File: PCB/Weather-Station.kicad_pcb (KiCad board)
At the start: 2 copper layers, 60 x 31.5 mm, 38 parts, among them J1 Biruta, J2 Power, J3 BH1750-FVI, J4 BME280, J5 Pluviometro, J6 Anemometro, J7 FTDI, J8 Conn_01x02, J9 Conn_01x02, SW1 SW_Push_SPDT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

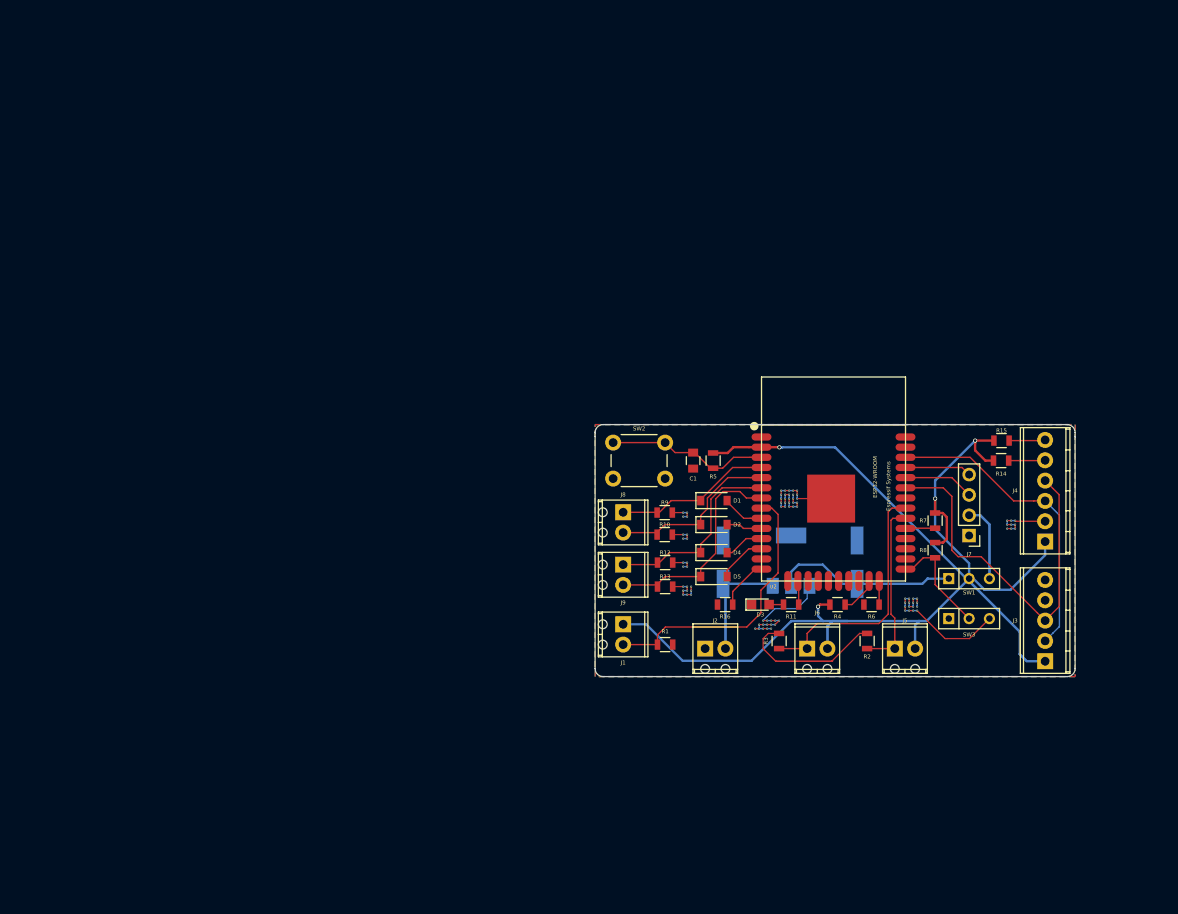
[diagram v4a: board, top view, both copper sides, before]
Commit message: Alterando as PCBs da estação para usar os ADCs e o DataLogger
Signed-off-by: Gustavo Costa <gustavocosta@ic.ufal.br>
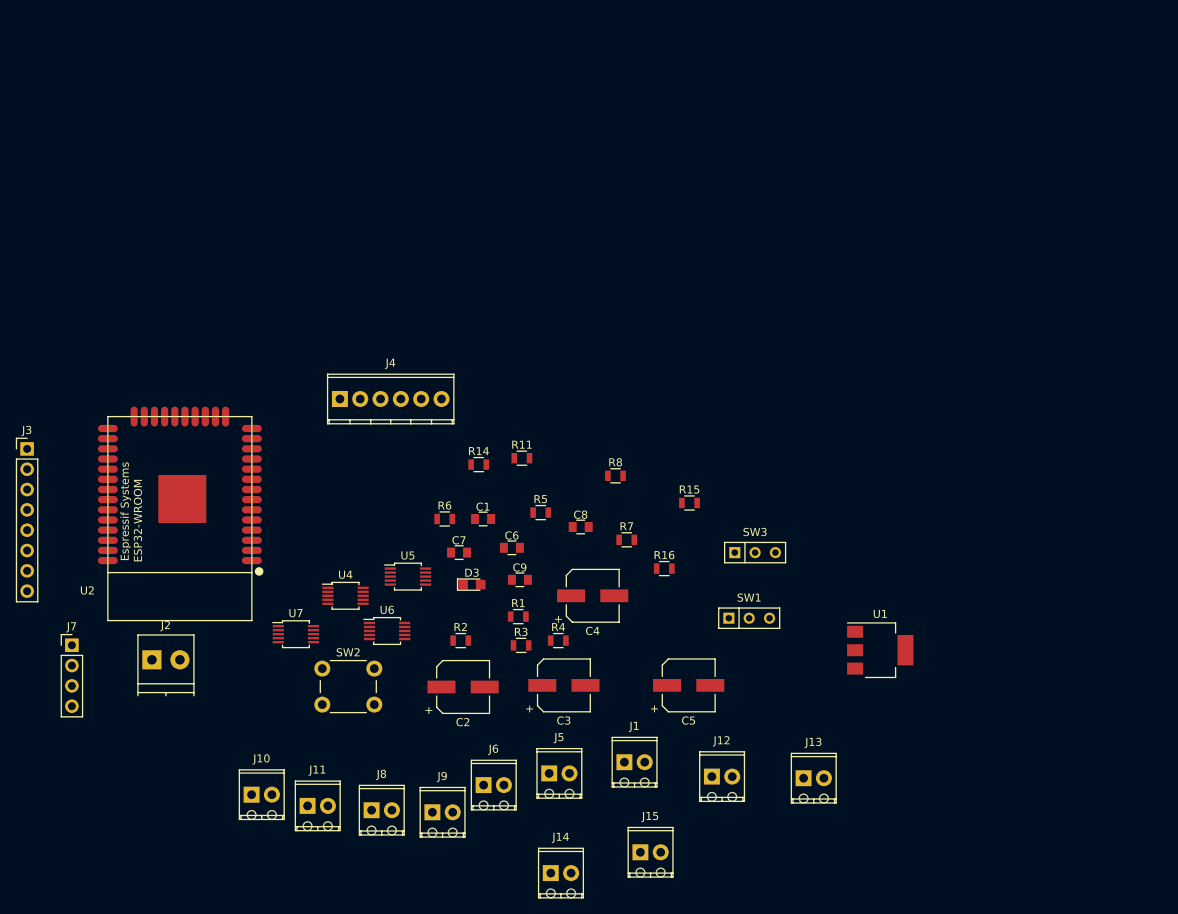
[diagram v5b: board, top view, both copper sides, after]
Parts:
- removed D1, D2, D4, D5: D, Diodes_SMD:D_SOD-123
- removed R10, R12, R13, R9: 1.5K, Resistors_SMD:R_0805
- added C4: 22μF, Capacitors_SMD:CP_Elec_6.3x7.7, F.Cu at (164.7, 102.4)
- added C5: 22μF, Capacitors_SMD:CP_Elec_6.3x7.7, F.Cu at (176.7, 113.6)
- added C6: 0.1uF, Capacitors_SMD:C_0805, F.Cu at (154.6, 96.4)
- added C7: 0.1uF, Capacitors_SMD:C_0805, F.Cu at (148.0, 97.0)
- added C8: 0.1uF, Capacitors_SMD:C_0805, F.Cu at (163.2, 93.8)
- added C9: 0.1uF, Capacitors_SMD:C_0805, F.Cu at (155.6, 100.4)
- added J10: Conn_01x02, TerminalBlock_Phoenix:TerminalBlock_Phoenix_MPT-2.54mm_2pol, F.Cu at (122.1, 127.3)
- added J11: Conn_01x02, TerminalBlock_Phoenix:TerminalBlock_Phoenix_MPT-2.54mm_2pol, F.Cu at (129.1, 128.7)
- added J12: Conn_01x02, TerminalBlock_Phoenix:TerminalBlock_Phoenix_MPT-2.54mm_2pol, F.Cu at (179.6, 125.0)
- added J13: Conn_01x02, TerminalBlock_Phoenix:TerminalBlock_Phoenix_MPT-2.54mm_2pol, F.Cu at (191.1, 125.2)
- added J14: Conn_01x02, TerminalBlock_Phoenix:TerminalBlock_Phoenix_MPT-2.54mm_2pol, F.Cu at (159.5, 137.1)
- added J15: Conn_01x02, TerminalBlock_Phoenix:TerminalBlock_Phoenix_MPT-2.54mm_2pol, F.Cu at (170.7, 134.5)
- added U4: ADS1115, Housings_SSOP:MSOP-10_3x3mm_Pitch0.5mm, F.Cu at (133.8, 102.4)
- added U5: ADS1115, Housings_SSOP:MSOP-10_3x3mm_Pitch0.5mm, F.Cu at (141.6, 100.0)
- added U6: ADS1115, Housings_SSOP:MSOP-10_3x3mm_Pitch0.5mm, F.Cu at (139.0, 106.8)
- added U7: ADS1115, Housings_SSOP:MSOP-10_3x3mm_Pitch0.5mm, F.Cu at (127.6, 107.2)
- C2, C3, U1: moved to F.Cu
- J2: footprint TerminalBlock_Phoenix:TerminalBlock_Phoenix_MPT-2.54mm_2pol -> TerminalBlock_Phoenix:TerminalBlock_Phoenix_PT-3.5mm_2pol
- J3: value BH1750-FVI -> DataLogger; footprint TerminalBlock_Phoenix:TerminalBlock_Phoenix_MPT-2.54mm_5pol -> Pin_Headers:Pin_Header_Straight_1x08_Pitch2.54mm
- moved J3 130.0 mm to (94.0, 84.0), turned to 0 degrees
- moved J7 113.0 mm to (99.6, 108.6), turned to 0 degrees
- moved J4 89.9 mm to (133.1, 77.8), turned to 0 degrees
- moved U2 81.9 mm to (113.1, 92.8), turned to 0 degrees
- moved J2 69.2 mm to (109.6, 110.4)
- moved R14 65.3 mm to (150.4, 86.0), turned to 0 degrees
- moved R6 54.4 mm to (146.2, 92.8), turned to 0 degrees
- moved R2 50.8 mm to (148.2, 108.0), turned to 0 degrees
- moved J8 48.7 mm to (137.1, 129.2), turned to 0 degrees
- moved SW2 46.0 mm to (130.9, 111.5)
- moved J5 45.9 mm to (159.3, 124.6)
- moved J6 43.9 mm to (151.1, 126.1)
- moved R8 41.0 mm to (167.6, 87.4), turned to 0 degrees
- moved R15 39.8 mm to (176.8, 90.8), turned to 0 degrees
- moved C3 39.8 mm to (161.1, 113.6), turned to 0 degrees
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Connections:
- net ADC1_CH4 renamed Net-(J1-Pad2)
- J3 pad 1: +3V3 -> CS
- J3 pad 2: Net-(J3-Pad2) -> MOSI
- J3 pad 3: Net-(J3-Pad3) -> MISO
- J3 pad 4: (no net) -> SCK
- J3 pad 5: GND -> SCL
- J4 pad 3: Net-(J3-Pad2) -> SCL
- J4 pad 4: Net-(J3-Pad3) -> SDA
- J8 pad 1: ADC1_CH0 -> Net-(J8-Pad1)
- J8 pad 2: ADC1_CH3 -> Net-(J8-Pad2)
- J9 pad 1: ADC1_CH6 -> Net-(J9-Pad1)
- J9 pad 2: ADC1_CH7 -> Net-(J9-Pad2)
- SW3 pad 1: (no net) -> Net-(SW3-Pad1)
- U2 pad 10: GPIO25 -> Net-(J6-Pad1)
- U2 pad 11: GPIO26 -> Net-(U2-Pad11)
- U2 pad 12: GPIO27 -> Net-(U2-Pad12)
- U2 pad 13: (no net) -> Net-(U2-Pad13)
- U2 pad 17: (no net) -> Net-(U2-Pad17)
- U2 pad 18: (no net) -> Net-(U2-Pad18)
- U2 pad 19: (no net) -> Net-(U2-Pad19)
- U2 pad 20: (no net) -> Net-(U2-Pad20)
- U2 pad 21: (no net) -> Net-(U2-Pad21)
- U2 pad 22: (no net) -> Net-(U2-Pad22)
- U2 pad 26: (no net) -> Net-(U2-Pad26)
- U2 pad 27: (no net) -> Net-(U2-Pad27)
- U2 pad 28: (no net) -> CS
- U2 pad 30: Net-(J5-Pad1) -> SCK
- U2 pad 31: Net-(J6-Pad1) -> MISO
- U2 pad 32: (no net) -> Net-(U2-Pad32)
- U2 pad 33: Net-(J3-Pad3) -> SDA
- U2 pad 36: Net-(J3-Pad2) -> SCL
- U2 pad 37: (no net) -> MOSI
- U2 pad 4: ADC1_CH0 -> Net-(U2-Pad4)
- U2 pad 5: ADC1_CH3 -> Net-(U2-Pad5)
- U2 pad 6: ADC1_CH6 -> Net-(U2-Pad6)
- U2 pad 7: ADC1_CH7 -> Net-(U2-Pad7)
- U2 pad 9: GPIO33 -> Net-(J5-Pad1)
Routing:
- net +3V3: track 165.8 -> 0.00 mm, vias 4 -> 0
- net GND: track 91.7 -> 0.00 mm, vias 86 -> 0
- net Net-(J3-Pad3): track 47.2 -> 0.00 mm
- net Net-(J3-Pad2): track 38.7 -> 0.00 mm
- net Net-(J1-Pad2): track 35.2 -> 0.00 mm
- net Net-(J6-Pad1): track 31.7 -> 0.00 mm
- net ADC1_CH7: track 27.4 -> 0.00 mm
- net ADC1_CH6: track 24.5 -> 0.00 mm
- net Net-(C3-Pad1): track 23.1 -> 0.00 mm
- net ADC1_CH3: track 22.0 -> 0.00 mm
- net Net-(J5-Pad1): track 21.6 -> 0.00 mm
- net Net-(C1-Pad2): track 20.5 -> 0.00 mm
- net ADC1_CH0: track 19.7 -> 0.00 mm
- net Net-(C2-Pad1): track 14.5 -> 0.00 mm
- net Net-(R8-Pad1): track 13.6 -> 0.00 mm
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- removed copper zone on B.Cu, net GND
- removed copper zone on F.Cu, net GND
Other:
- board outline removed

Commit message: Iniciado PCB
Signed-off-by: Gustavo Costa <gustavocosta@ic.ufal.br>
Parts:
- added U3: AP1117-33, TO_SOT_Packages_SMD:SOT-223, B.Cu at (143.8, 62.8)
- C2, C3, C4, C5, J3, U1: moved to B.Cu
- moved J7 89.8 mm to (180.8, 70.2), turned to 270 degrees
- moved J3 86.2 mm to (179.9, 76.5), turned to 90 degrees
- moved J1 74.9 mm to (126.2, 61.5), turned to 270 degrees
- moved J5 64.1 mm to (126.2, 69.7), turned to 270 degrees
- moved U1 61.0 mm to (143.8, 87.2)
- moved SW2 55.0 mm to (131.2, 56.5), turned to 180 degrees
- moved J6 54.4 mm to (126.2, 77.7), turned to 270 degrees
- moved C5 54.1 mm to (143.8, 70.8)
- moved U7 53.3 mm to (179.7, 95.8)
- moved U2 52.9 mm to (151.8, 56.8), turned to 180 degrees
- moved J4 52.6 mm to (184.0, 64.7), turned to 90 degrees
- moved C4 52.3 mm to (143.8, 54.5)
- moved SW1 49.4 mm to (171.2, 57.5), turned to 180 degrees
- moved R1 49.0 mm to (137.9, 59.2), turned to 180 degrees
- moved R3 48.0 mm to (138.0, 64.0), turned to 180 degrees
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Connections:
- SW3 pad 1: Net-(SW3-Pad1) -> (no net)
- U2 pad 11: Net-(U2-Pad11) -> (no net)
- U2 pad 12: Net-(U2-Pad12) -> (no net)
- U2 pad 13: Net-(U2-Pad13) -> (no net)
- U2 pad 17: Net-(U2-Pad17) -> (no net)
- U2 pad 18: Net-(U2-Pad18) -> (no net)
- U2 pad 19: Net-(U2-Pad19) -> (no net)
- U2 pad 20: Net-(U2-Pad20) -> (no net)
- U2 pad 21: Net-(U2-Pad21) -> (no net)
- U2 pad 22: Net-(U2-Pad22) -> (no net)
- U2 pad 26: Net-(U2-Pad26) -> (no net)
- U2 pad 27: Net-(U2-Pad27) -> (no net)
- U2 pad 32: Net-(U2-Pad32) -> (no net)
- U2 pad 4: Net-(U2-Pad4) -> (no net)
- U2 pad 5: Net-(U2-Pad5) -> (no net)
- U2 pad 6: Net-(U2-Pad6) -> (no net)
- U2 pad 7: Net-(U2-Pad7) -> (no net)
- U4 pad 2: Net-(U4-Pad2) -> (no net)
- U5 pad 2: Net-(U5-Pad2) -> (no net)
- U6 pad 2: Net-(U6-Pad2) -> (no net)
- U7 pad 2: Net-(U7-Pad2) -> (no net)
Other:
- board outline added: 65 x 60 mm

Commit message: Fazendo pcb
Signed-off-by: Gustavo Costa <gustavocosta@ic.ufal.br>
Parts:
- added R10: 10k, Resistors_SMD:R_0805, F.Cu at (160.8, 82.2)
- added R9: 10k, Resistors_SMD:R_0805, F.Cu at (160.8, 86.5)
- moved C2 24.8 mm to (143.8, 54.5)
- moved C3 24.8 mm to (143.8, 70.8)
- moved U1 24.8 mm to (143.8, 62.5)
- moved C4 24.5 mm to (143.8, 79.0)
- moved C5 24.5 mm to (143.8, 95.2)
- moved U3 24.5 mm to (143.8, 87.2)
- moved SW3 20.1 mm to (169.2, 72.5), turned to 0 degrees
- moved J7 19.0 mm to (174.0, 52.5)
- moved SW1 16.4 mm to (178.0, 72.5), turned to 0 degrees
- moved R7 1.00 mm to (165.5, 63.0)
- moved R8 1.00 mm to (165.5, 68.0)
- moved R3 0.25 mm to (138.0, 64.2)
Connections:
- U4 pad 4: Net-(J8-Pad2) -> Net-(J8-Pad1)
- U4 pad 5: Net-(J8-Pad1) -> Net-(J8-Pad2)
- U4 pad 6: Net-(J9-Pad2) -> Net-(J9-Pad1)
- U4 pad 7: Net-(J9-Pad1) -> Net-(J9-Pad2)
- U5 pad 4: Net-(J10-Pad2) -> Net-(J10-Pad1)
- U5 pad 5: Net-(J10-Pad1) -> Net-(J10-Pad2)
- U5 pad 6: Net-(J11-Pad2) -> Net-(J11-Pad1)
- U5 pad 7: Net-(J11-Pad1) -> Net-(J11-Pad2)
- U6 pad 4: Net-(J12-Pad2) -> Net-(J12-Pad1)
- U6 pad 5: Net-(J12-Pad1) -> Net-(J12-Pad2)
- U6 pad 6: Net-(J13-Pad2) -> Net-(J13-Pad1)
- U6 pad 7: Net-(J13-Pad1) -> Net-(J13-Pad2)
- U7 pad 4: Net-(J14-Pad2) -> Net-(J14-Pad1)
- U7 pad 5: Net-(J14-Pad1) -> Net-(J14-Pad2)
- U7 pad 6: Net-(J15-Pad2) -> Net-(J15-Pad1)
- U7 pad 7: Net-(J15-Pad1) -> Net-(J15-Pad2)
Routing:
- net Net-(C2-Pad1): track 0.00 -> 63.1 mm
- net Net-(J6-Pad1): track 0.00 -> 24.0 mm
- net +5V: track 0.00 -> 23.2 mm
- net Net-(J5-Pad1): track 0.00 -> 19.9 mm
- net Net-(C1-Pad2): track 0.00 -> 19.6 mm
- net Net-(J1-Pad2): track 0.00 -> 19.0 mm
- net Net-(J14-Pad1): track 0.00 -> 13.1 mm
- net Net-(J13-Pad2): track 0.00 -> 12.4 mm
- net Net-(J8-Pad1): track 0.00 -> 12.3 mm
- net Net-(J15-Pad2): track 0.00 -> 12.0 mm
- net Net-(J9-Pad2): track 0.00 -> 11.9 mm
- net Net-(J12-Pad1): track 0.00 -> 11.9 mm
- net Net-(J10-Pad1): track 0.00 -> 11.8 mm
- net Net-(J11-Pad2): track 0.00 -> 11.8 mm
- net Net-(C3-Pad1): track 0.00 -> 10.9 mm
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
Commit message: Finalizando PCB
Signed-off-by: Gustavo <gustavocosta@ic.ufal.br>
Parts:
- moved SW1 13.6 mm to (173.2, 59.7), turned to 90 degrees
- moved SW3 5.32 mm to (173.2, 68.9), turned to 90 degrees
- moved R9 2.94 mm to (163.0, 84.6), turned to 0 degrees
- moved R10 2.34 mm to (163.0, 81.6), turned to 0 degrees
- moved R6 1.43 mm to (157.6, 73.6), turned to 270 degrees
- moved R4 0.87 mm to (155.2, 73.6), turned to 270 degrees
- moved SW2 0.50 mm to (131.8, 56.5)
- moved C1 0.20 mm to (134.8, 53.8)
- moved R5 0.20 mm to (138.2, 53.8)
- moved R11 0.10 mm to (147.4, 73.8)
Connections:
- SW3 pad 1: (no net) -> Net-(SW3-Pad1)
- U2 pad 11: (no net) -> Net-(U2-Pad11)
- U2 pad 12: (no net) -> Net-(U2-Pad12)
- U2 pad 13: (no net) -> Net-(U2-Pad13)
- U2 pad 17: (no net) -> Net-(U2-Pad17)
- U2 pad 18: (no net) -> Net-(U2-Pad18)
- U2 pad 19: (no net) -> Net-(U2-Pad19)
- U2 pad 20: (no net) -> Net-(U2-Pad20)
- U2 pad 21: (no net) -> Net-(U2-Pad21)
- U2 pad 22: (no net) -> Net-(U2-Pad22)
- U2 pad 26: (no net) -> Net-(U2-Pad26)
- U2 pad 27: (no net) -> Net-(U2-Pad27)
- U2 pad 32: (no net) -> Net-(U2-Pad32)
- U2 pad 4: (no net) -> Net-(U2-Pad4)
- U2 pad 5: (no net) -> Net-(U2-Pad5)
- U2 pad 6: (no net) -> Net-(U2-Pad6)
- U2 pad 7: (no net) -> Net-(U2-Pad7)
- U4 pad 2: (no net) -> Net-(U4-Pad2)
- U4 pad 3: (no net) -> GND
- U5 pad 2: (no net) -> Net-(U5-Pad2)
- U5 pad 3: (no net) -> GND
- U6 pad 2: (no net) -> Net-(U6-Pad2)
- U6 pad 3: (no net) -> GND
- U7 pad 2: (no net) -> Net-(U7-Pad2)
- U7 pad 3: (no net) -> GND
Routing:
- net +3V3: track 0.00 -> 170.1 mm
- net SDA: track 0.00 -> 147.7 mm, vias 0 -> 3
- net SCL: track 0.00 -> 145.9 mm, vias 0 -> 3
- net +5V: track 23.2 -> 136.3 mm, vias 0 -> 5
- net GND: track 0.00 -> 77.2 mm, vias 0 -> 15
- net MOSI: track 0.00 -> 37.5 mm, vias 0 -> 1
- net Net-(C3-Pad1): track 10.9 -> 46.6 mm
- net MISO: track 0.00 -> 28.6 mm, vias 0 -> 1
- net CS: track 0.00 -> 27.9 mm, vias 0 -> 2
- net SCK: track 0.00 -> 27.6 mm, vias 0 -> 1
- net Net-(R8-Pad1): track 3.75 -> 14.6 mm, vias 0 -> 1
- net RXD: track 0.00 -> 9.87 mm, vias 0 -> 1
- net TXD: track 0.00 -> 7.36 mm, vias 0 -> 1
- net Net-(J4-Pad6): track 0.00 -> 5.93 mm
- net Net-(J7-Pad2): track 0.00 -> 5.40 mm
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- added copper zone on B.Cu, net GND
- added copper zone on F.Cu, net GND
